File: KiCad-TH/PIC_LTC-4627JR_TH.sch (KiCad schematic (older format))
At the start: 17 parts, among them J1 Conn_01x05_Male, J2 Conn_01x04, Q1 Q_NPN_EBC, Q2 Q_NPN_EBC, Q3 Q_NPN_EBC, Q4 Q_NPN_EBC, Q5 Q_NPN_EBC, U1 PIC16F18344-P

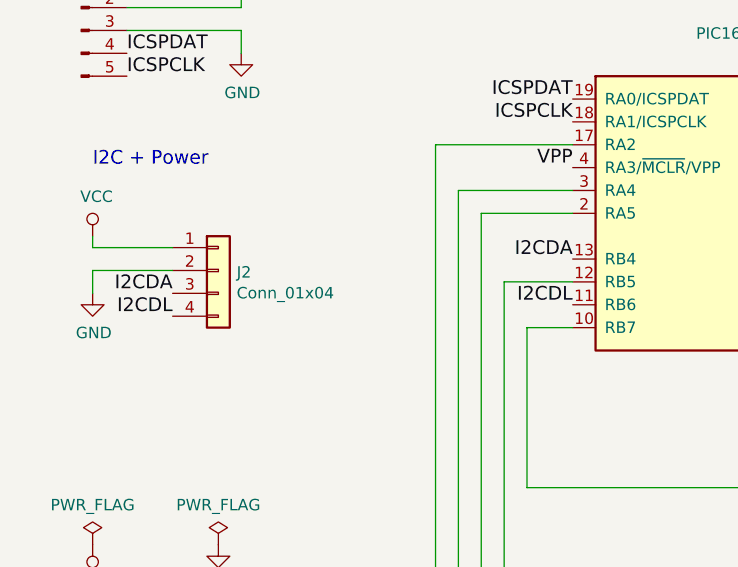
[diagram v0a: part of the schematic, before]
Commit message: Deleted all the tracks to start again.
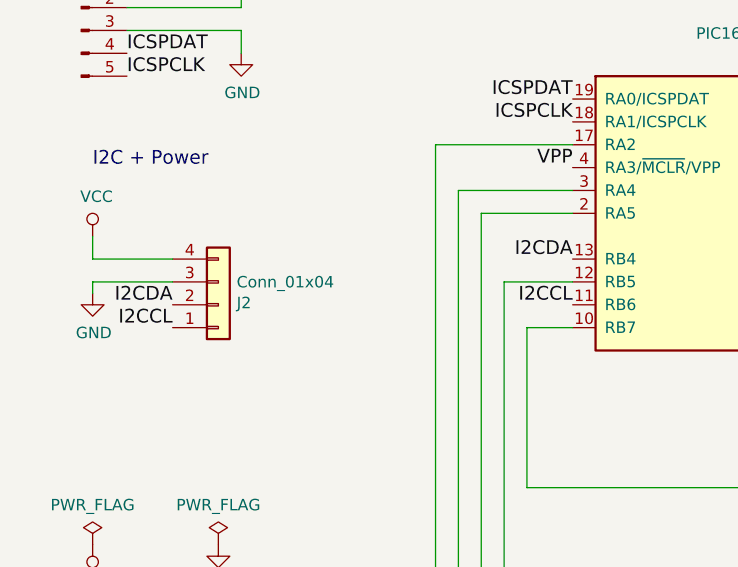
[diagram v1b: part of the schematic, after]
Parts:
- J1: footprint (none) -> Connectors_JST:JST_XH_B05B-XH-A_05x2.50mm_Straight
- J2: footprint (none) -> Connectors_JST:JST_PH_B4B-PH-K_04x2.00mm_Straight
- L1: footprint (none) -> LTC-4627JR:LTC-4627JR
- Q1, Q2, Q3, Q4, Q5: footprint (none) -> TO_SOT_Packages_THT:TO-92_Inline_Narrow_Oval
- R1, R2, R3, R4, R5, R6, R7, R8: footprint (none) -> Resistors_THT:R_Axial_DIN0207_L6.3mm_D2.5mm_P7.62mm_Horizontal
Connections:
- net GND: now also J2.3 (Pin_3); no longer J2.2 (Pin_2)
- net I2CDA: now also J2.2 (Pin_2); no longer J2.3 (Pin_3)
- net VCC: now also J2.4 (Pin_4); no longer J2.1 (Pin_1)
- net I2CDL renamed I2CCL
- net I2CCL: now also J2.1 (Pin_1); no longer J2.4 (Pin_4)
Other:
- moved on the sheet: J2
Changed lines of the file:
@@
 F 0 "J1" H 1356 2878 50  0000 C CNN
 F 1 "Conn_01x05_Male" H 1356 2787 50  0000 C CNN
-F 2 "" H 1250 2500 50  0001 C CNN
+F 2 "Connectors_JST:JST_XH_B05B-XH-A_05x2.50mm_Straight" H 1250 2500 50  0001 C CNN
 F 3 "" H 1250 2500 50  0001 C CNN
 	1    1250 2500
@@
 L Conn_01x04 J2
 U 1 1 59CC41F4
-P 1850 3550
-F 0 "J2" H 1930 3542 50  0000 L CNN
-F 1 "Conn_01x04" H 1930 3451 50  0000 L CNN
-F 2 "" H 1850 3550 50  0001 C CNN
-F 3 "" H 1850 3550 50  0001 C CNN
-	1    1850 3550
-	1    0    0    -1
+P 1850 3700
+F 0 "J2" H 1930 3692 50  0000 L CNN
+F 1 "Conn_01x04" H 1930 3601 50  0000 L CNN
+F 2 "Connectors_JST:JST_PH_B4B-PH-K_04x2.00mm_Straight" H 1850 3700 50  0001 C CNN
+F 3 "" H 1850 3700 50  0001 C CNN
+	1    1850 3700
+	1    0    0    1
 $EndComp
 $Comp
@@
 F 0 "R1" V 5693 2100 50  0000 C CNN
 F 1 "120" V 5784 2100 50  0000 C CNN
-F 2 "" V 5830 2100 50  0001 C CNN
+F 2 "Resistors_THT:R_Axial_DIN0207_L6.3mm_D2.5mm_P7.62mm_Horizontal" V 5830 2100 50  0001 C CNN
 F 3 "" H 5900 2100 50  0001 C CNN
 	1    5900 2100
@@
 F 0 "Q5" H 4691 4546 50  0000 L CNN
 F 1 "Q_NPN_EBC" H 4691 4455 50  0000 L CNN
-F 2 "" H 4700 4600 50  0001 C CNN
+F 2 "TO_SOT_Packages_THT:TO-92_Inline_Narrow_Oval" H 4700 4600 50  0001 C CNN
 F 3 "" H 4500 4500 50  0001 C CNN
 	1    4500 4500
@@
 I2CDA
 Text Label 3400 3700 2    60   ~ 0
-I2CDL
-Text Label 1650 3650 2    60   ~ 0
-I2CDA
-Text Label 1650 3750 2    60   ~ 0
-I2CDL
-Wire Wire Line
-	1650 3550 1300 3550
-Wire Wire Line
-	1300 3550 1300 3650
-Wire Wire Line
-	1650 3450 1300 3450
-Wire Wire Line
-	1300 3450 1300 3400
+I2CCL
 Text Notes 1450 2050 0    60   ~ 0
 PICkit 3
@@
 F 0 "R2" V 5693 2400 50  0000 C CNN
 F 1 "120" V 5784 2400 50  0000 C CNN
-F 2 "" V 5830 2400 50  0001 C CNN
+F 2 "Resistors_THT:R_Axial_DIN0207_L6.3mm_D2.5mm_P7.62mm_Horizontal" V 5830 2400 50  0001 C CNN
 F 3 "" H 5900 2400 50  0001 C CNN
 	1    5900 2400
@@
 F 0 "R3" V 5693 2700 50  0000 C CNN
 F 1 "120" V 5784 2700 50  0000 C CNN
-F 2 "" V 5830 2700 50  0001 C CNN
+F 2 "Resistors_THT:R_Axial_DIN0207_L6.3mm_D2.5mm_P7.62mm_Horizontal" V 5830 2700 50  0001 C CNN
 F 3 "" H 5900 2700 50  0001 C CNN
 	1    5900 2700
@@
 F 0 "R4" V 5693 3000 50  0000 C CNN
 F 1 "120" V 5784 3000 50  0000 C CNN
-F 2 "" V 5830 3000 50  0001 C CNN
+F 2 "Resistors_THT:R_Axial_DIN0207_L6.3mm_D2.5mm_P7.62mm_Horizontal" V 5830 3000 50  0001 C CNN
 F 3 "" H 5900 3000 50  0001 C CNN
 	1    5900 3000
@@
 F 0 "R5" V 5693 3300 50  0000 C CNN
 F 1 "120" V 5784 3300 50  0000 C CNN
-F 2 "" V 5830 3300 50  0001 C CNN
+F 2 "Resistors_THT:R_Axial_DIN0207_L6.3mm_D2.5mm_P7.62mm_Horizontal" V 5830 3300 50  0001 C CNN
 F 3 "" H 5900 3300 50  0001 C CNN
 	1    5900 3300
@@
 F 0 "R6" V 5693 3600 50  0000 C CNN
 F 1 "120" V 5784 3600 50  0000 C CNN
-F 2 "" V 5830 3600 50  0001 C CNN
+F 2 "Resistors_THT:R_Axial_DIN0207_L6.3mm_D2.5mm_P7.62mm_Horizontal" V 5830 3600 50  0001 C CNN
 F 3 "" H 5900 3600 50  0001 C CNN
 	1    5900 3600
@@
 F 0 "R7" V 5693 3900 50  0000 C CNN
 F 1 "120" V 5784 3900 50  0000 C CNN
-F 2 "" V 5830 3900 50  0001 C CNN
+F 2 "Resistors_THT:R_Axial_DIN0207_L6.3mm_D2.5mm_P7.62mm_Horizontal" V 5830 3900 50  0001 C CNN
 F 3 "" H 5900 3900 50  0001 C CNN
 	1    5900 3900
@@
 F 0 "R8" V 5693 4200 50  0000 C CNN
 F 1 "120" V 5784 4200 50  0000 C CNN
-F 2 "" V 5830 4200 50  0001 C CNN
+F 2 "Resistors_THT:R_Axial_DIN0207_L6.3mm_D2.5mm_P7.62mm_Horizontal" V 5830 4200 50  0001 C CNN
 F 3 "" H 5900 4200 50  0001 C CNN
 	1    5900 4200
@@
 F 0 "Q4" H 4691 5296 50  0000 L CNN
 F 1 "Q_NPN_EBC" H 4691 5205 50  0000 L CNN
-F 2 "" H 4700 5350 50  0001 C CNN
+F 2 "TO_SOT_Packages_THT:TO-92_Inline_Narrow_Oval" H 4700 5350 50  0001 C CNN
 F 3 "" H 4500 5250 50  0001 C CNN
 	1    4500 5250
@@
 F 0 "Q3" H 4691 6046 50  0000 L CNN
 F 1 "Q_NPN_EBC" H 4691 5955 50  0000 L CNN
-F 2 "" H 4700 6100 50  0001 C CNN
+F 2 "TO_SOT_Packages_THT:TO-92_Inline_Narrow_Oval" H 4700 6100 50  0001 C CNN
 F 3 "" H 4500 6000 50  0001 C CNN
 	1    4500 6000
@@
 F 0 "Q2" H 4691 6796 50  0000 L CNN
 F 1 "Q_NPN_EBC" H 4691 6705 50  0000 L CNN
-F 2 "" H 4700 6850 50  0001 C CNN
+F 2 "TO_SOT_Packages_THT:TO-92_Inline_Narrow_Oval" H 4700 6850 50  0001 C CNN
 F 3 "" H 4500 6750 50  0001 C CNN
 	1    4500 6750
@@
 F 0 "Q1" H 4691 7546 50  0000 L CNN
 F 1 "Q_NPN_EBC" H 4691 7455 50  0000 L CNN
-F 2 "" H 4700 7600 50  0001 C CNN
+F 2 "TO_SOT_Packages_THT:TO-92_Inline_Narrow_Oval" H 4700 7600 50  0001 C CNN
 F 3 "" H 4500 7500 50  0001 C CNN
 	1    4500 7500
@@
 F 0 "L1" H 6050 5487 60  0000 C CNN
 F 1 "LTC-4627JR" H 6050 5381 60  0000 C CNN
-F 2 "" H 6050 5400 60  0001 C CNN
+F 2 "LTC-4627JR:LTC-4627JR" H 6050 5400 60  0001 C CNN
 F 3 "" H 6050 5400 60  0001 C CNN
 	1    6050 5400
@@
 Wire Wire Line
 	7400 2100 6050 2100
+Wire Wire Line
+	1650 3500 1300 3500
+Wire Wire Line
+	1300 3500 1300 3400
+Wire Wire Line
+	1650 3600 1300 3600
+Wire Wire Line
+	1300 3600 1300 3650
+Text Label 1650 3700 2    60   ~ 0
+I2CDA
+Text Label 1650 3800 2    60   ~ 0
+I2CCL
 $EndSCHEMATC

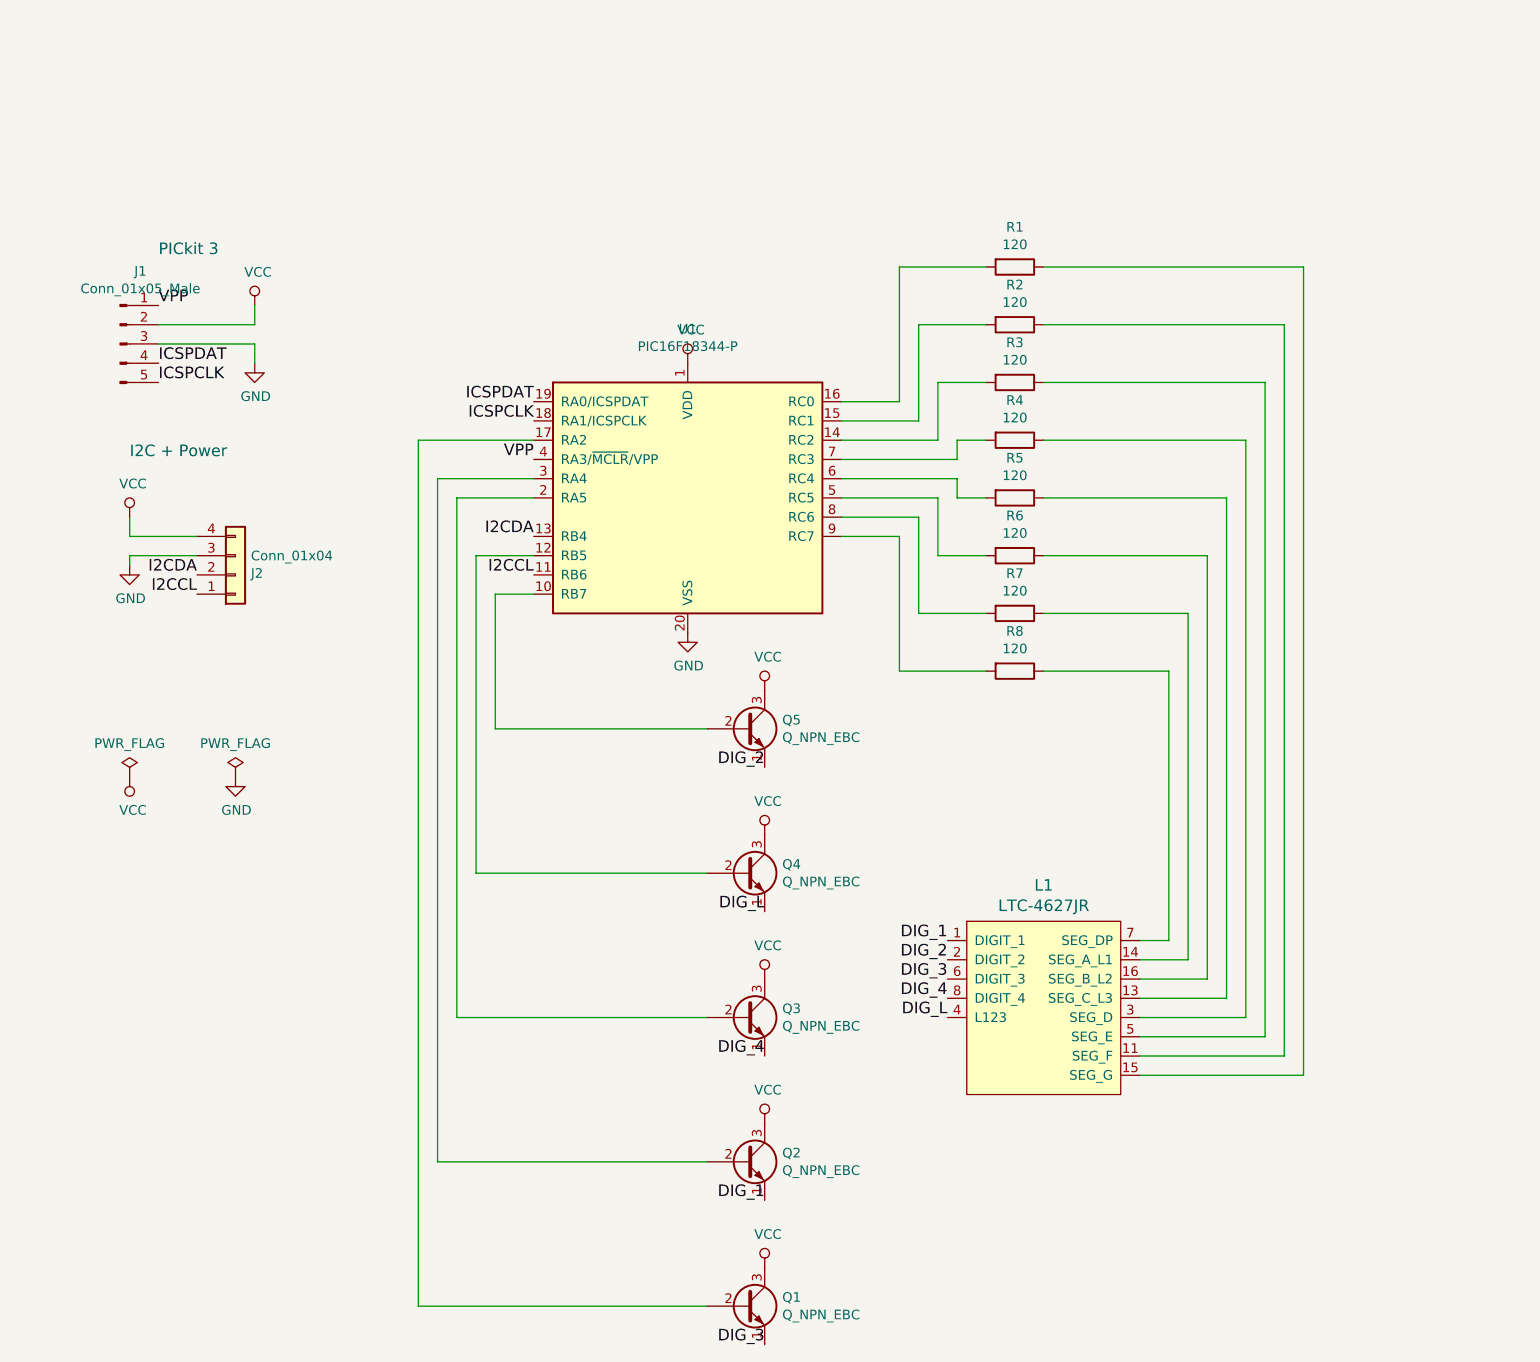
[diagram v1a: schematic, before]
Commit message: Fix transistor footprint and add 1kOhm resistor between PIC and transistor base
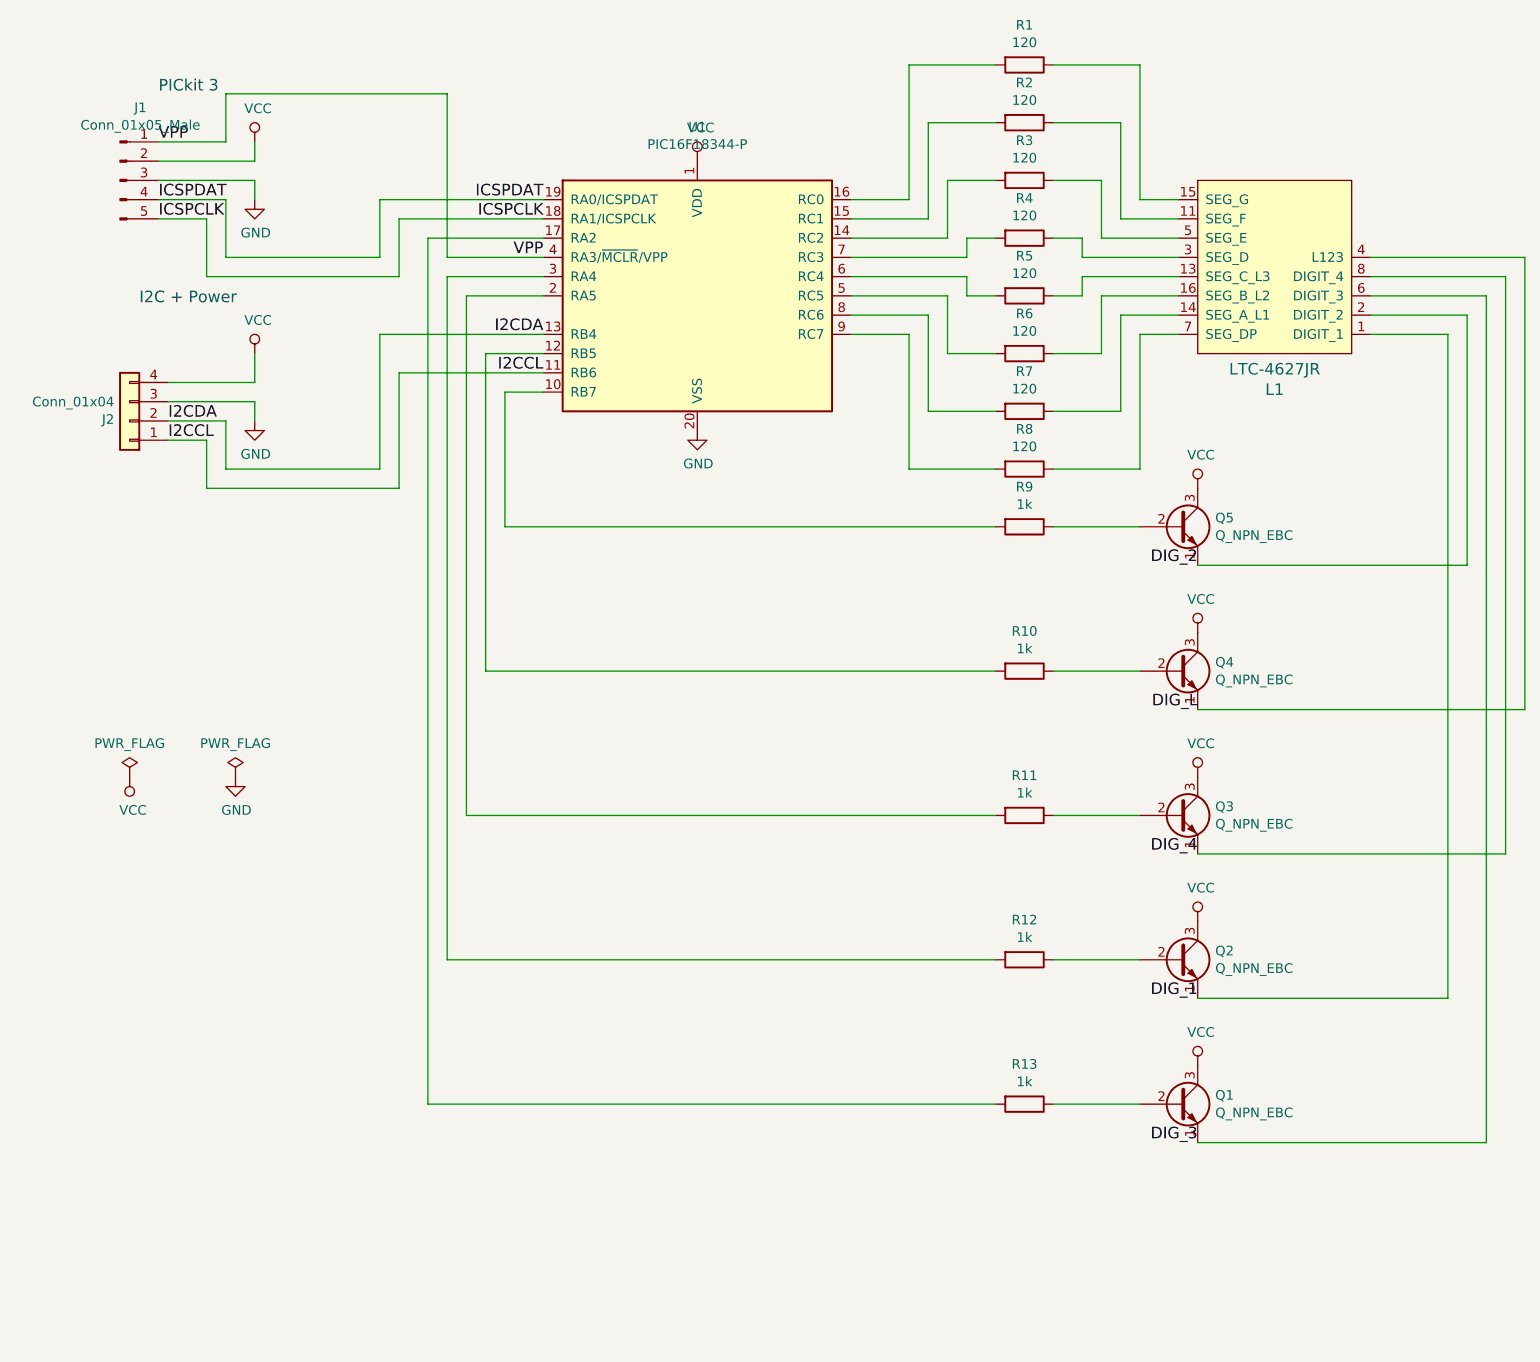
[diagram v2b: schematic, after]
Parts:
- added R10, R11, R12, R13, R9: 1k, Resistors_THT:R_Axial_DIN0207_L6.3mm_D2.5mm_P10.16mm_Horizontal, symbol R
- J1: footprint Connectors_JST:JST_XH_B05B-XH-A_05x2.50mm_Straight -> Pin_Headers:Pin_Header_Straight_1x05_Pitch2.54mm
- R1, R2, R3, R4, R5, R6, R7, R8: footprint Resistors_THT:R_Axial_DIN0207_L6.3mm_D2.5mm_P7.62mm_Horizontal -> Resistors_THT:R_Axial_DIN0207_L6.3mm_D2.5mm_P10.16mm_Horizontal
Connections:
- net at U1.10 (RB7): now also R9.2; no longer Q5.2 (B)
- net at U1.12 (RB5): now also R10.2; no longer Q4.2 (B)
- net at U1.17 (RA2): now also R13.2; no longer Q1.2 (B)
- net at U1.2 (RA5): now also R11.2; no longer Q3.2 (B)
- net at U1.3 (RA4): now also R12.2; no longer Q2.2 (B)
- new net: Q5.2 (B), R9.1
- new net: Q4.2 (B), R10.1
- new net: Q3.2 (B), R11.1
- new net: Q2.2 (B), R12.1
- new net: Q1.2 (B), R13.1
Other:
- moved on the sheet: J1, J2, L1, Q1, Q2, Q3, Q4, Q5, R1, R2, R3, R4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

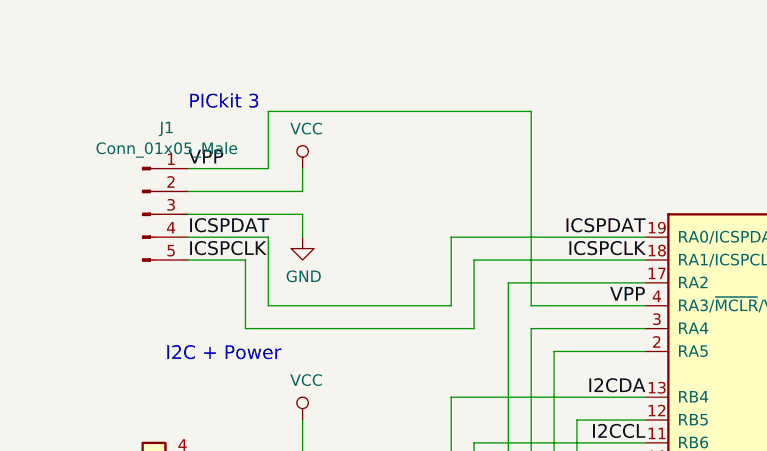
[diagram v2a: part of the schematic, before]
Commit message: Add pull-up resistor to Vpp as per PICkit 3 manual
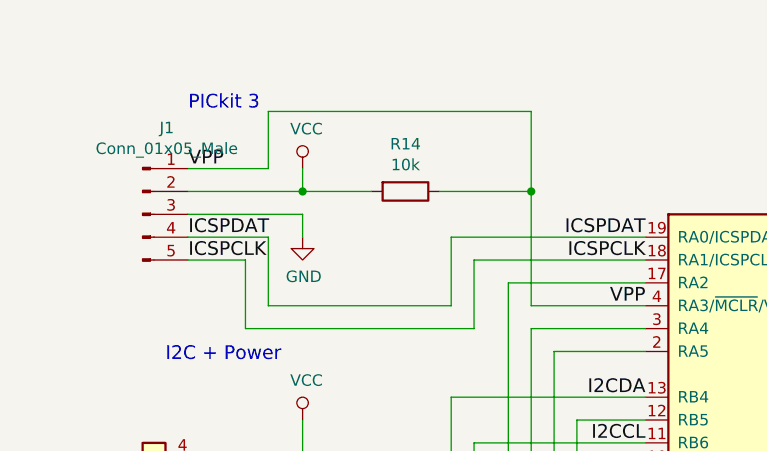
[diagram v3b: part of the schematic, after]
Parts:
- added R14: 10k, Resistors_THT:R_Axial_DIN0207_L6.3mm_D2.5mm_P10.16mm_Horizontal, symbol R
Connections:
- net VCC: now also R14.2
- net VPP: now also R14.1
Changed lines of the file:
@@
 	1950 1650 1450 1650
 Wire Wire Line
-	1450 1550 1950 1550
+	1450 1550 2250 1550
 Wire Wire Line
 	1950 1550 1950 1450
@@
 Wire Wire Line
 	1700 3000 1500 3000
+$Comp
+L R R14
+U 1 1 59D0296A
+P 2400 1550
+F 0 "R14" V 2193 1550 50  0000 C CNN
+F 1 "10k" V 2284 1550 50  0000 C CNN
+F 2 "Resistors_THT:R_Axial_DIN0207_L6.3mm_D2.5mm_P10.16mm_Horizontal" V 2330 1550 50  0001 C CNN
+F 3 "" H 2400 1550 50  0001 C CNN
+	1    2400 1550
+	0    1    1    0
+$EndComp
+Wire Wire Line
+	2550 1550 2950 1550
+Connection ~ 2950 1550
+Connection ~ 1950 1550
 $EndSCHEMATC
